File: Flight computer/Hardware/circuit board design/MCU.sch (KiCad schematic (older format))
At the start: 31 parts, among them J1 Conn_01x05, U11 ATSAML21J18B-AUT, U7 W74M64FV, Y3 16MHz

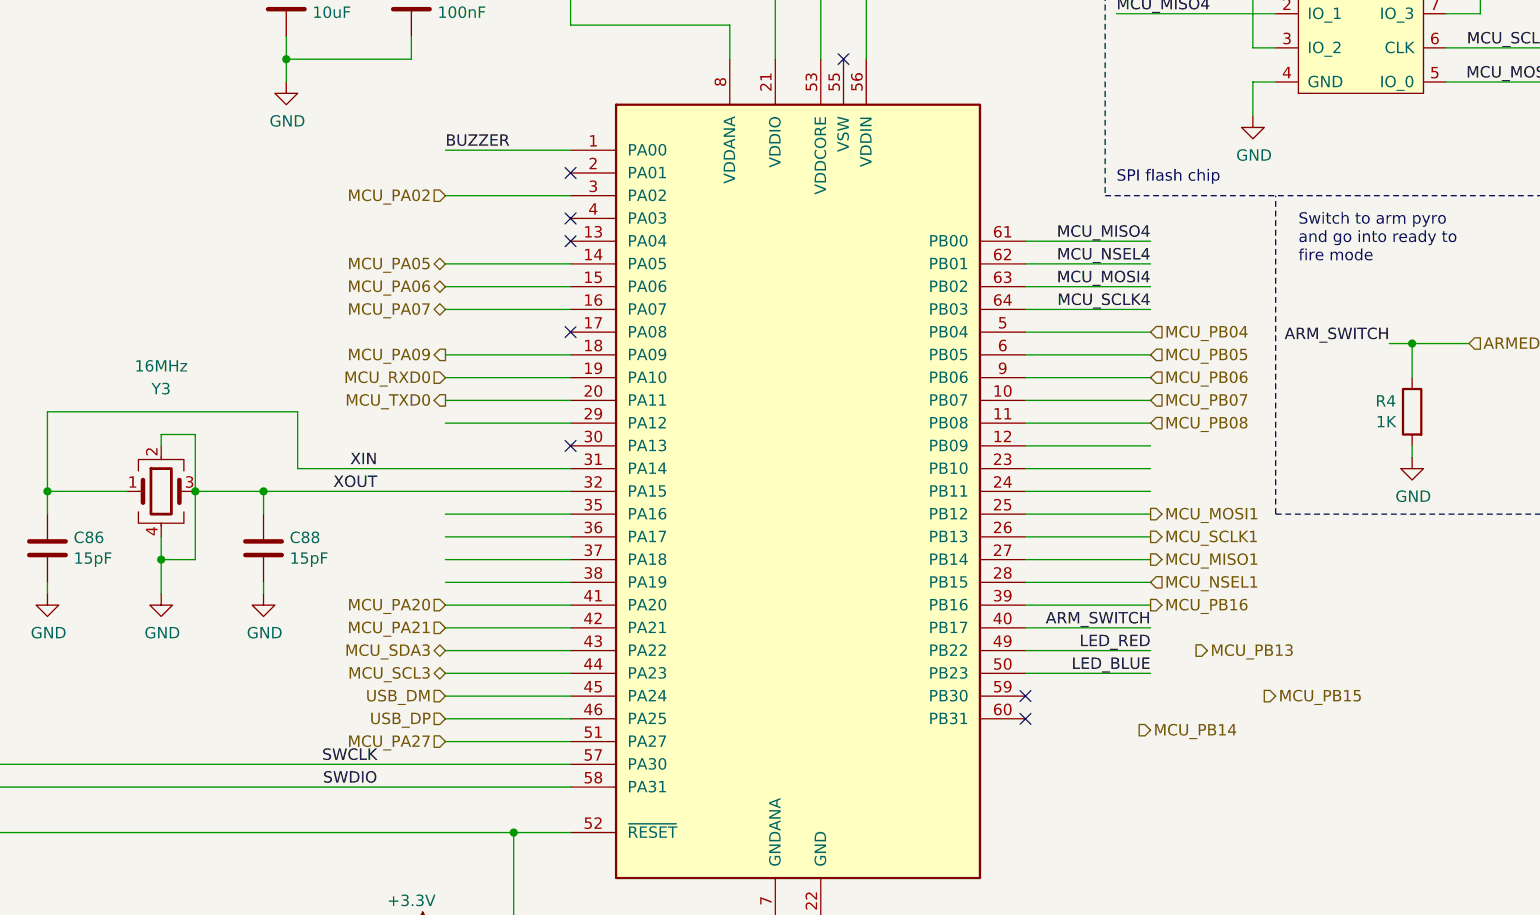
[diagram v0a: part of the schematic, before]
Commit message: Did Major reworking of ports
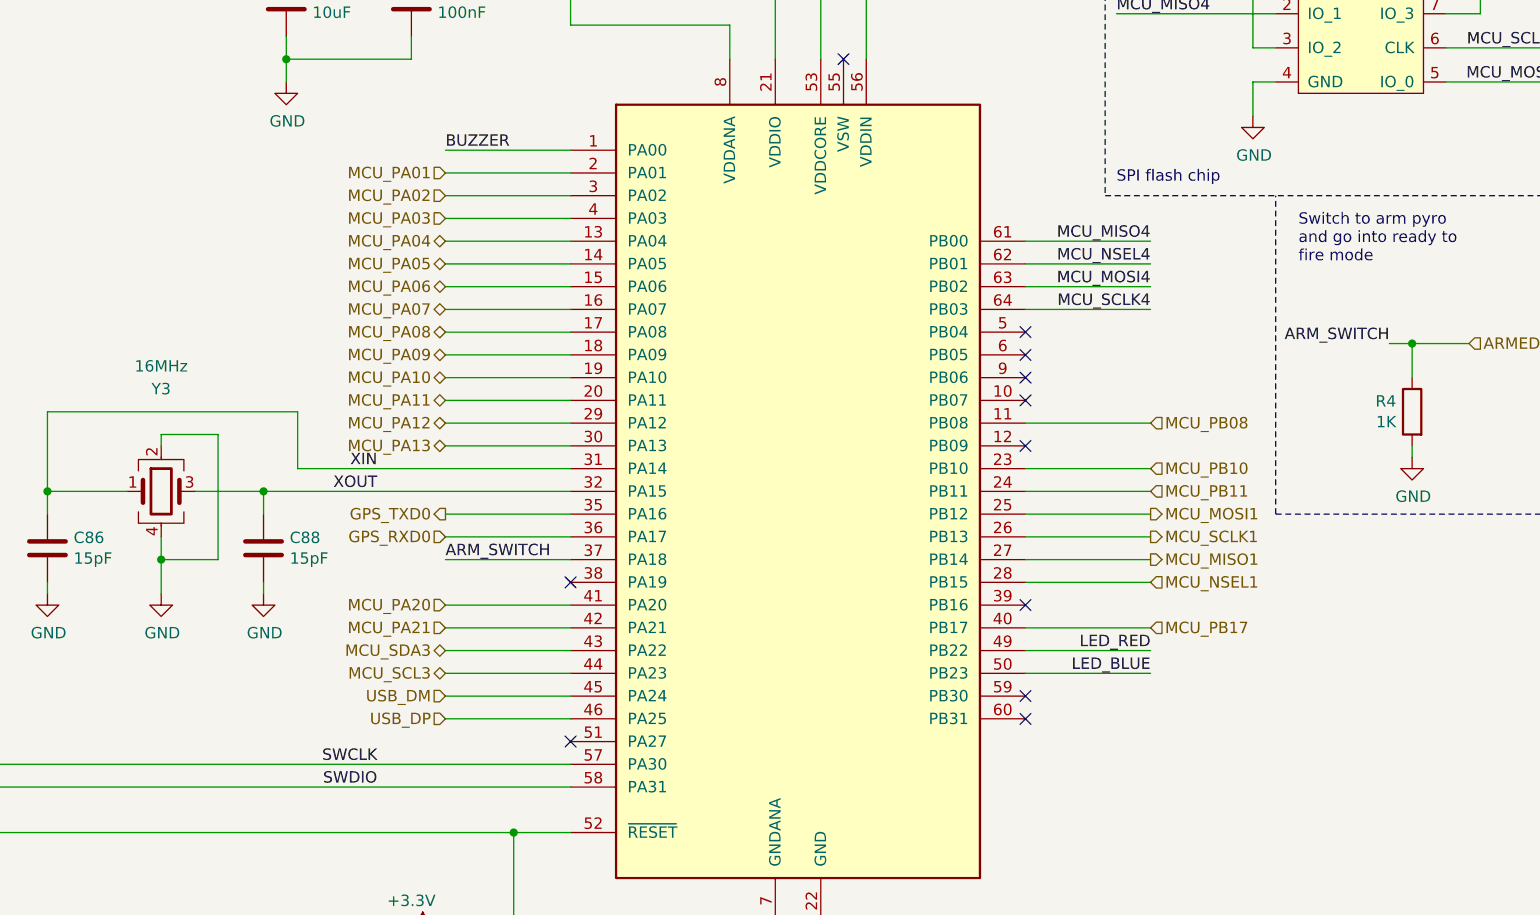
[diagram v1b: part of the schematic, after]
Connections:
- net labels added: GPS_RXD0, GPS_TXD0, MCU_PA01, MCU_PA03, MCU_PA04, MCU_PA08, MCU_PA10, MCU_PA11, MCU_PA12, MCU_PA13, MCU_PB10, MCU_PB11, MCU_PB17
- net labels removed: MCU_PA27, MCU_PB04, MCU_PB05, MCU_PB06, MCU_PB07, MCU_PB13, MCU_PB14, MCU_PB15, MCU_PB16, MCU_RXD0, MCU_TXD0
- wire segments 186 -> 182
- no-connect marks 8 -> 11
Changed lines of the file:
@@
 $EndComp
-Wire Wire Line
-	3150 4400 2800 4400
 Wire Wire Line
 	2800 4400 2800 4500
@@
 	2250 5700 2250 4450
 Wire Wire Line
-	5100 4600 4550 4600
-Wire Wire Line
-	5100 4700 4550 4700
-Wire Wire Line
-	5100 4800 4550 4800
-Wire Wire Line
 	5100 5200 4550 5200
 Wire Wire Line
@@
 Wire Wire Line
 	5100 4000 4550 4000
-Text HLabel 4550 4000 0    50   Output ~ 0
-MCU_TXD0
-Text HLabel 4550 3900 0    50   Input ~ 0
-MCU_RXD0
+Text HLabel 4550 4500 0    50   Output ~ 0
+GPS_TXD0
+Text HLabel 4550 4600 0    50   Input ~ 0
+GPS_RXD0
 Text HLabel 4550 3100 0    50   Input ~ 0
 MCU_PA02
@@
 	8100 2600 8100 2750
 Wire Wire Line
-	5100 3400 4550 3400
-Wire Wire Line
 	5100 3500 4550 3500
 Wire Wire Line
 	5100 3600 4550 3600
-Text HLabel 4550 3400 0    50   BiDi ~ 0
-MCU_PA05
 Text HLabel 4550 3500 0    50   BiDi ~ 0
 MCU_PA06
@@
 Wire Wire Line
 	5100 3800 4550 3800
-Text HLabel 4550 3800 0    50   Output ~ 0
-MCU_PA09
 Wire Wire Line
 	7100 3500 7650 3500
@@
 Text Label 9450 2600 2    50   ~ 0
 MCU_MOSI4
-Text HLabel 7650 4100 2    50   Input ~ 0
-MCU_PB08
 $Comp
 L power:GND #PWR021
@@
 Wire Wire Line
 	4550 5000 5100 5000
-Wire Wire Line
-	4550 5500 5100 5500
-Wire Wire Line
-	5100 4100 4550 4100
-Wire Wire Line
-	5100 4500 4550 4500
 Wire Notes Line
 	7450 1500 7450 3100
@@
 MCU_NSEL4
 Wire Wire Line
-	7100 4100 7650 4100
-Wire Wire Line
-	7100 4200 7650 4200
-Wire Wire Line
-	7100 4300 7650 4300
-Wire Wire Line
 	8950 2450 9450 2450
-Wire Wire Line
-	7650 4400 7100 4400
 Wire Wire Line
 	7650 4500 7100 4500
@@
 Buzzer\n
 Wire Wire Line
-	7100 3700 7650 3700
-Wire Wire Line
-	7100 3800 7650 3800
-Text HLabel 7650 3700 2    50   Input ~ 0
-MCU_PB04
-Text HLabel 7650 3800 2    50   Input ~ 0
-MCU_PB05
-Wire Wire Line
 	7100 4600 7650 4600
 Wire Wire Line
 	7100 4700 7650 4700
-Text HLabel 7850 5100 2    50   Output ~ 0
-MCU_PB13
-Text HLabel 7600 5450 2    50   Output ~ 0
-MCU_PB14
-Wire Wire Line
-	7100 3900 7650 3900
-Wire Wire Line
-	7100 4000 7650 4000
-Text HLabel 7650 3900 2    50   Input ~ 0
-MCU_PB06
-Text HLabel 7650 4000 2    50   Input ~ 0
-MCU_PB07
 Wire Wire Line
 	7100 4800 7650 4800
-Wire Wire Line
-	7100 4900 7650 4900
-Text HLabel 8150 5300 2    50   Output ~ 0
-MCU_PB15
-Text HLabel 7650 4900 2    50   Output ~ 0
-MCU_PB16
-Text HLabel 4550 5500 0    50   Input ~ 0
-MCU_PA27
 Text Label 4250 5600 2    50   ~ 0
 SWCLK
-NoConn ~ 5100 3700
-NoConn ~ 5100 3300
-NoConn ~ 5100 3200
 Wire Notes Line
 	11050 1500 11050 6150
@@
 Text Notes 9600 6100 0    50   ~ 0
 Two indicator LEDs
-NoConn ~ 5100 3000
 Wire Wire Line
 	1000 1150 900  1150
@@
 Text Notes 1000 2350 0    50   ~ 0
 Mechanical mounting holes
-NoConn ~ 5100 4200
-Wire Wire Line
-	7100 5000 7650 5000
-Text Label 7650 5000 2    50   ~ 0
+Wire Wire Line
+	5100 4700 4550 4700
+Text Label 4550 4700 0    50   ~ 0
 ARM_SWITCH
 Text Label 8700 3750 2    50   ~ 0
@@
 Wire Wire Line
 	3750 4500 3750 4400
-Wire Wire Line
-	3450 4400 3750 4400
 $Comp
 L power:GND #PWR018
@@
 $EndComp
 $Comp
-L Device:Crystal_GND24 Y3
-U 1 1 5D6EF892
-P 3300 4400
-F 0 "Y3" H 3300 4850 50  0000 C CNN
-F 1 "16MHz" H 3300 4950 50  0000 C CNN
-F 2 "Crystal:Crystal_SMD_2520-4Pin_2.5x2.0mm" H 3300 4400 50  0001 C CNN
-F 3 "https://docs-emea.rs-online.com/webdocs/15dc/0900766b815dc75d.pdf" H 3300 4400 50  0001 C CNN
-	1    3300 4400
-	1    0    0    -1
-$EndComp
-$Comp
 L MCU_Microchip_SAML:ATSAML21J18B-AUT U11
 U 1 1 5D748E67
@@
 	1    0    0    -1
 $EndComp
-NoConn ~ 7100 5300
 Text HLabel 7650 4700 2    50   Output ~ 0
 MCU_MISO1
@@
 MCU_MOSI1
 Wire Wire Line
-	3300 4200 3300 4150
-Wire Wire Line
-	3300 4150 3450 4150
-Wire Wire Line
-	3450 4700 3300 4700
-Wire Wire Line
-	3450 4150 3450 4400
-Wire Wire Line
-	3450 4400 3450 4700
-Connection ~ 3450 4400
-Wire Wire Line
-	3300 4600 3300 4700
-Wire Wire Line
 	3300 4700 3300 4850
 Connection ~ 3300 4700
 Text Label 7650 3300 2    50   ~ 0
 MCU_MISO4
-NoConn ~ 7100 5400
 Text Label 4550 2900 0    50   ~ 0
 BUZZER
@@
 Wire Wire Line
 	4550 2900 5100 2900
+Wire Wire Line
+	5100 3700 4550 3700
+Text HLabel 4550 3700 0    50   BiDi ~ 0
+MCU_PA08
+Text HLabel 4550 3800 0    50   BiDi ~ 0
+MCU_PA09
+Text HLabel 4550 3900 0    50   BiDi ~ 0
+MCU_PA10
+Text HLabel 4550 4000 0    50   BiDi ~ 0
+MCU_PA11
+NoConn ~ 7100 4900
+NoConn ~ 7100 4200
+NoConn ~ 5100 4800
+Wire Wire Line
+	4550 4500 5100 4500
+Wire Wire Line
+	4550 4600 5100 4600
+Wire Wire Line
+	3300 4600 3300 4700
+Wire Wire Line
+	3450 4400 3750 4400
+Wire Wire Line
+	3300 4200 3300 4150
+Wire Wire Line
+	3150 4400 2800 4400
+$Comp
+L Device:Crystal_GND24 Y3
+U 1 1 5D6EF892
+P 3300 4400
+F 0 "Y3" H 3300 4850 50  0000 C CNN
+F 1 "16MHz" H 3300 4950 50  0000 C CNN
+F 2 "Crystal:Crystal_SMD_2520-4Pin_2.5x2.0mm" H 3300 4400 50  0001 C CNN
+F 3 "https://docs-emea.rs-online.com/webdocs/15dc/0900766b815dc75d.pdf" H 3300 4400 50  0001 C CNN
+	1    3300 4400
+	1    0    0    -1
+$EndComp
+Wire Wire Line
+	3550 4150 3550 4700
+Wire Wire Line
+	3300 4700 3550 4700
+Wire Wire Line
+	3300 4150 3550 4150
+Wire Wire Line
+	7100 4100 7650 4100
+Text HLabel 7650 4100 2    50   Input ~ 0
+MCU_PB08
+Text HLabel 4550 3400 0    50   BiDi ~ 0
+MCU_PA05
+Wire Wire Line
+	5100 3400 4550 3400
+Wire Wire Line
+	5100 3300 4550 3300
+Text HLabel 4550 3300 0    50   BiDi ~ 0
+MCU_PA04
+Wire Wire Line
+	5100 4100 4550 4100
+Wire Wire Line
+	5100 4200 4550 4200
+Text HLabel 4550 4100 0    50   BiDi ~ 0
+MCU_PA12
+Text HLabel 4550 4200 0    50   BiDi ~ 0
+MCU_PA13
+Wire Wire Line
+	7100 4400 7650 4400
+Text HLabel 7650 4400 2    50   Input ~ 0
+MCU_PB11
+Wire Wire Line
+	7100 5000 7650 5000
+Text HLabel 7650 5000 2    50   Input ~ 0
+MCU_PB17
+Wire Wire Line
+	5100 3000 4550 3000
+Text HLabel 4550 3000 0    50   Input ~ 0
+MCU_PA01
+Wire Wire Line
+	5100 3200 4550 3200
+Text HLabel 4550 3200 0    50   Input ~ 0
+MCU_PA03
+NoConn ~ 7100 4000
+NoConn ~ 7100 3900
+NoConn ~ 7100 3800
+NoConn ~ 7100 3700
+NoConn ~ 7100 5400
+NoConn ~ 7100 5300
+Wire Wire Line
+	7100 4300 7650 4300
+Text HLabel 7650 4300 2    50   Input ~ 0
+MCU_PB10
+NoConn ~ 5100 5500
 $EndSCHEMATC

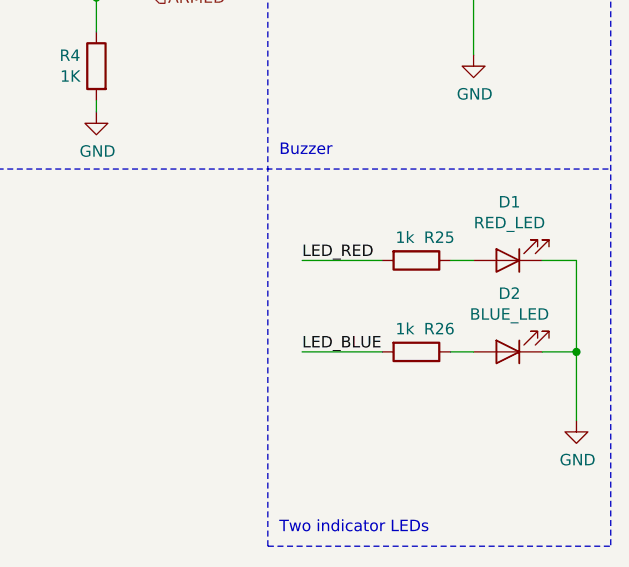
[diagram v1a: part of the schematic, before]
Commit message: added in the footprint for the 6 terminal block
routed the RF section with the 434 antenna
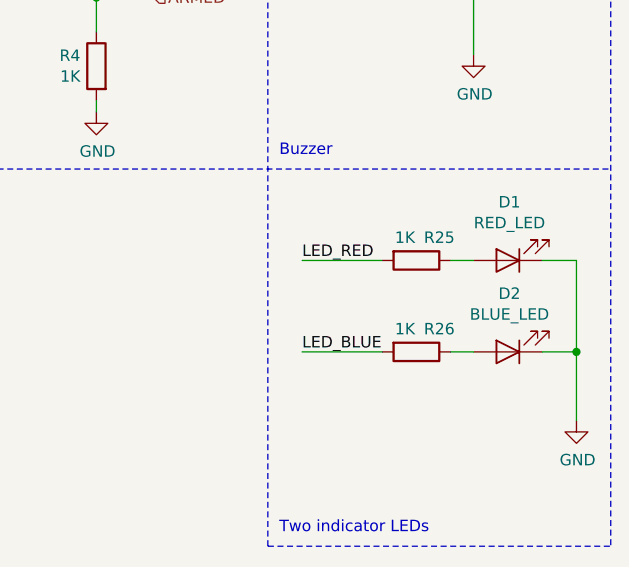
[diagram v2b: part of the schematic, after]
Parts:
- R25, R26: value 1k -> 1K
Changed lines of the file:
@@
 P 10200 4900
 F 0 "R25" V 10100 5000 50  0000 C CNN
-F 1 "1k" V 10100 4850 50  0000 C CNN
+F 1 "1K" V 10100 4850 50  0000 C CNN
 F 2 "Resistor_SMD:R_0603_1608Metric" V 10130 4900 50  0001 C CNN
 F 3 "~" H 10200 4900 50  0001 C CNN
@@
 P 10200 5300
 F 0 "R26" V 10100 5400 50  0000 C CNN
-F 1 "1k" V 10100 5250 50  0000 C CNN
+F 1 "1K" V 10100 5250 50  0000 C CNN
 F 2 "Resistor_SMD:R_0603_1608Metric" V 10130 5300 50  0001 C CNN
 F 3 "~" H 10200 5300 50  0001 C CNN

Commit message: only 2 or 3 connections left to route
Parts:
- removed R4: 1K, Resistor_SMD:R_0603_1608Metric, symbol Device:R
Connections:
- net ARMED: no longer names the net of U11.37 (PA18)
- no-connect marks 11 -> 12
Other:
- note removed: "Switch to arm pyro \nand go into ready to \nfire mode"
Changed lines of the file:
@@
 $Descr A4 11693 8268
 encoding utf-8
-Sheet 7 7
+Sheet 6 7
 Title ""
 Date "2019-09-09"
@@
 Mechanical mounting holes
 Wire Wire Line
-	5100 4700 4550 4700
-Text Label 4550 4700 0    50   ~ 0
-ARM_SWITCH
-Text Label 8700 3750 2    50   ~ 0
-ARM_SWITCH
-Wire Wire Line
-	8700 3750 8800 3750
-Wire Wire Line
-	8800 3750 8800 3900
-Connection ~ 8800 3750
-Wire Wire Line
-	8800 3750 9050 3750
-$Comp
-L power:GND #PWR017
-U 1 1 5D83136F
-P 8800 4250
-F 0 "#PWR017" H 8800 4000 50  0001 C CNN
-F 1 "GND" H 8805 4077 50  0000 C CNN
-F 2 "" H 8800 4250 50  0001 C CNN
-F 3 "" H 8800 4250 50  0001 C CNN
-	1    8800 4250
-	1    0    0    -1
-$EndComp
-Wire Notes Line
-	8200 4500 8200 3100
-Wire Notes Line
-	8200 4500 11050 4500
-Text Notes 8300 3400 0    50   ~ 0
-Switch to arm pyro \nand go into ready to \nfire mode
-Wire Wire Line
-	8800 4200 8800 4250
-Wire Wire Line
 	1350 4750 1450 4750
 Wire Wire Line
@@
 Wire Notes Line
 	9550 3100 9550 6150
-Text HLabel 9050 3750 2    50   Input ~ 0
-ARMED
 $Comp
 L power:GND #PWR085
@@
 F 3 "~" H 1150 4550 50  0001 C CNN
 	1    1150 4550
-	-1   0    0    -1
-$EndComp
-$Comp
-L Device:R R4
-U 1 1 5D854BB0
-P 8800 4050
-F 0 "R4" H 8870 4096 50  0000 L CNN
-F 1 "1K" H 8870 4005 50  0000 L CNN
-F 2 "Resistor_SMD:R_0603_1608Metric" V 8730 4050 50  0001 C CNN
-F 3 "~" H 8800 4050 50  0001 C CNN
-	1    8800 4050
 	-1   0    0    -1
 $EndComp
@@
 Text HLabel 7650 4800 2    50   Input ~ 0
 MCU_NSEL1
-Text HLabel 7650 4600 2    50   Output ~ 0
-MCU_SCLK1
-Text HLabel 7650 4500 2    50   Output ~ 0
-MCU_MOSI1
 Wire Wire Line
 	3300 4700 3300 4850
@@
 Wire Wire Line
 	7100 4100 7650 4100
-Text HLabel 7650 4100 2    50   Input ~ 0
-MCU_PB08
 Text HLabel 4550 3400 0    50   BiDi ~ 0
 MCU_PA05
@@
 Wire Wire Line
 	7100 4400 7650 4400
-Text HLabel 7650 4400 2    50   Input ~ 0
-MCU_PB11
 Wire Wire Line
 	7100 5000 7650 5000
@@
 Wire Wire Line
 	7100 4300 7650 4300
+NoConn ~ 5100 5500
 Text HLabel 7650 4300 2    50   Input ~ 0
 MCU_PB10
-NoConn ~ 5100 5500
+Text HLabel 7650 4400 2    50   Input ~ 0
+MCU_PB11
+Text HLabel 7650 4100 2    50   Input ~ 0
+MCU_PB08
+Text HLabel 7650 4500 2    50   Output ~ 0
+MCU_MOSI1
+Text HLabel 7650 4600 2    50   Output ~ 0
+MCU_SCLK1
+NoConn ~ 5100 4700
 $EndSCHEMATC

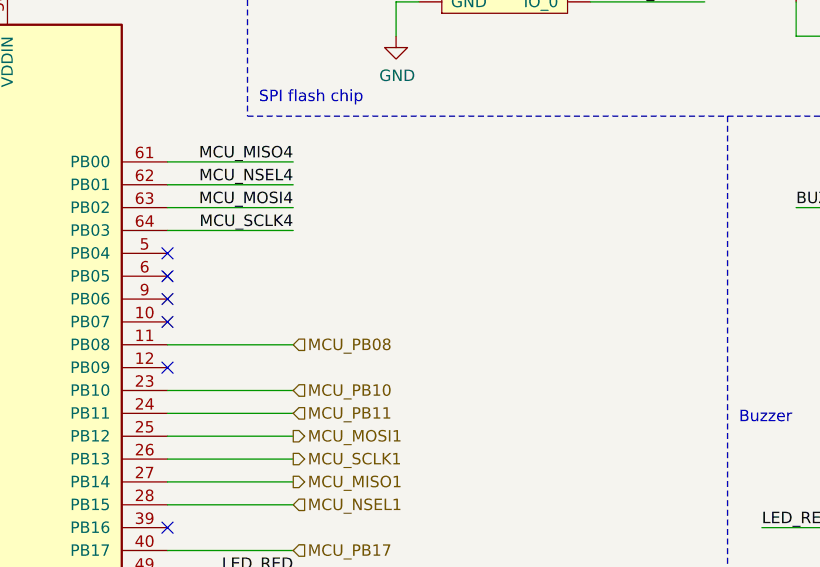
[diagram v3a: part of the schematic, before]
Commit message: cleaned up redundent overlapping tracks
also added a 4 header pins for unused mcu pins to the circuit. Not added to board layout yet.
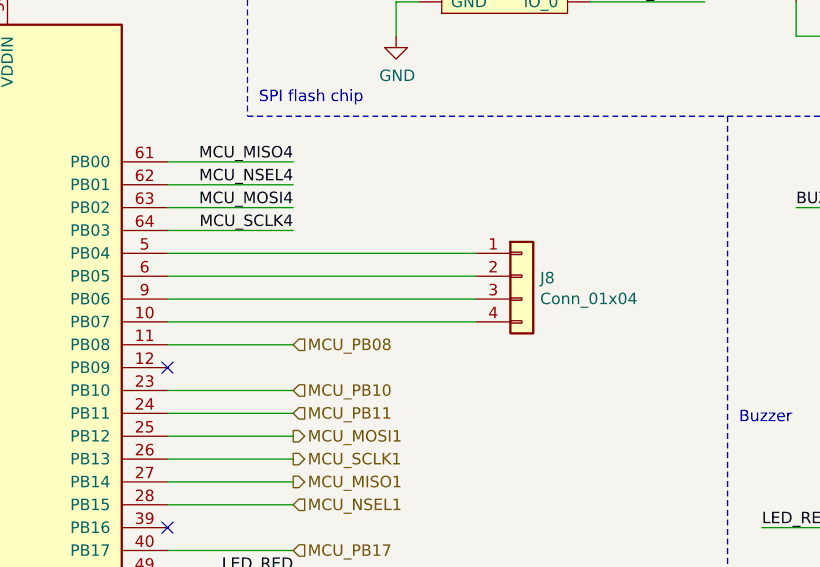
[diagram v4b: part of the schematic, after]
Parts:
- added J8: Conn_01x04, Connector_PinHeader_2.54mm:PinHeader_1x05_P2.54mm_Vertical, symbol Connector_Generic:Conn_01x04
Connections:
- net at U11.10 (PB07): now also J8.4 (Pin_4)
- net at U11.5 (PB04): now also J8.1 (Pin_1)
- net at U11.6 (PB05): now also J8.2 (Pin_2)
- net at U11.9 (PB06): now also J8.3 (Pin_3)
- no-connect marks 12 -> 8
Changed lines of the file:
@@
-	1    0    0    -1
-$EndComp
-$Comp
-L MCU_Microchip_SAML:ATSAML21J18B-AUT U11
-U 1 1 5D748E67
-P 6100 4400
-F 0 "U11" H 6100 2411 50  0000 C CNN
-F 1 "ATSAML21J18B-AUT" H 6400 2250 50  0000 C CNN
-F 2 "Package_QFP:TQFP-64_10x10mm_P0.5mm" H 7300 6200 50  0001 C CNN
-F 3 "http://ww1.microchip.com/downloads/en/DeviceDoc/60001477A.pdf" H 6100 4400 50  0001 C CNN
-F 4 "4.15" H 6100 4400 50  0001 C CNN "Cost"
-F 5 "https://www.mouser.co.uk/ProductDetail/Microchip-Technology/ATSAML21J18B-AUT?qs=RCSZh%2F2c5ne9n8KccuU8Bw%3D%3D" H 6100 4400 50  0001 C CNN "Purchase link"
-	1    6100 4400
 	1    0    0    -1
 $EndComp
@@
 Text HLabel 4550 3200 0    50   Input ~ 0
 MCU_PA03
-NoConn ~ 7100 4000
-NoConn ~ 7100 3900
-NoConn ~ 7100 3800
-NoConn ~ 7100 3700
 NoConn ~ 7100 5400
 NoConn ~ 7100 5300
@@
 MCU_SCLK1
 NoConn ~ 5100 4700
+$Comp
+L Connector_Generic:Conn_01x04 J8
+U 1 1 5DB0330A
+P 8650 3800
+F 0 "J8" H 8730 3792 50  0000 L CNN
+F 1 "Conn_01x04" H 8730 3701 50  0000 L CNN
+F 2 "Connector_PinHeader_2.54mm:PinHeader_1x05_P2.54mm_Vertical" H 8650 3800 50  0001 C CNN
+F 3 "~" H 8650 3800 50  0001 C CNN
+	1    8650 3800
+	1    0    0    -1
+$EndComp
+$Comp
+L MCU_Microchip_SAML:ATSAML21J18B-AUT U11
+U 1 1 5D748E67
+P 6100 4400
+F 0 "U11" H 6100 2411 50  0000 C CNN
+F 1 "ATSAML21J18B-AUT" H 6400 2250 50  0000 C CNN
+F 2 "Package_QFP:TQFP-64_10x10mm_P0.5mm" H 7300 6200 50  0001 C CNN
+F 3 "http://ww1.microchip.com/downloads/en/DeviceDoc/60001477A.pdf" H 6100 4400 50  0001 C CNN
+F 4 "4.15" H 6100 4400 50  0001 C CNN "Cost"
+F 5 "https://www.mouser.co.uk/ProductDetail/Microchip-Technology/ATSAML21J18B-AUT?qs=RCSZh%2F2c5ne9n8KccuU8Bw%3D%3D" H 6100 4400 50  0001 C CNN "Purchase link"
+	1    6100 4400
+	1    0    0    -1
+$EndComp
+Wire Wire Line
+	7100 3700 8450 3700
+Wire Wire Line
+	8450 3800 7100 3800
+Wire Wire Line
+	7100 3900 8450 3900
+Wire Wire Line
+	7100 4000 8450 4000
 $EndSCHEMATC
